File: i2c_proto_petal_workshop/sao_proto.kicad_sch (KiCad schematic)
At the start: 26 parts, among them J1 Simple_Addon_v2, J2 Programming: Jump Me, J3 GPIOs, J4 Jumpers, M1 Vibro Motor, M2 Solenoid, M3 Buzzer Motor, Q1 2N2222 (NPN), Q2 2N2222 (NPN), Q3 2N2222 (NPN)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

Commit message: updated schematic
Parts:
- added R6: 10K, symbol Device:R
- M1: value Vibro Motor -> Vibro Motor PWM
- M2: value Solenoid -> Solenoid GPIO Trigger
- M3: value Buzzer Motor -> Buzzer Motor GPIO
- R1: value 330R ? -> 68R ?
- R3: value 220R ? -> 1K
- R4: value 1K ? -> 1K
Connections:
- net PC0: now also J1.6 (GPIO2); no longer J1.5 (GPIO1), J2.2 (Pin_2)
- net PC3: no longer U1.13 (PC3)
- net PD5: no longer SW1.2
- net PD7: now also SW1.2, R6.2
- net VCC: now also R6.1
- net at J3.1 (Pin_1), R5.1: now also J1.5 (GPIO1), J2.2 (Pin_2); no longer J1.6 (GPIO2)
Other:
- note added: "CH32V003 Pin config: PC0 GPIO 2 input from Rpi (record signal), triggers in code RED LED on PD0 PC4 Vibro Output PC5 Solenoid Ouput PC6 Buzzer Output PD0 REC LED output (hardwired) PD1 PROGRAMMING input (hardwired) PD7 Push button input (pulled up with 10K resistor) GPIO 1 output from Rpi (metro signal) - doesn't come into the board, it just triggers the metronome LED"
- note added: "Solenoid currently unused!"
- note removed: "CH32V003 Pin config: PC0 GPIO 1 input from Rpi (record signal) PC4 Vibro Input PC5 Solenoid Input PC6 Buzzer Input PD0 REC LED output (hardwired) PD1 PROGRAMMING input (hardwired) Note: GPIO 2 input from Rpi doesn't come into the board, it just triggers the metronome LED"
- moved on the sheet: D2, D3, D4, J3, M2, M3, Q2, Q3, R1, R3, SW1

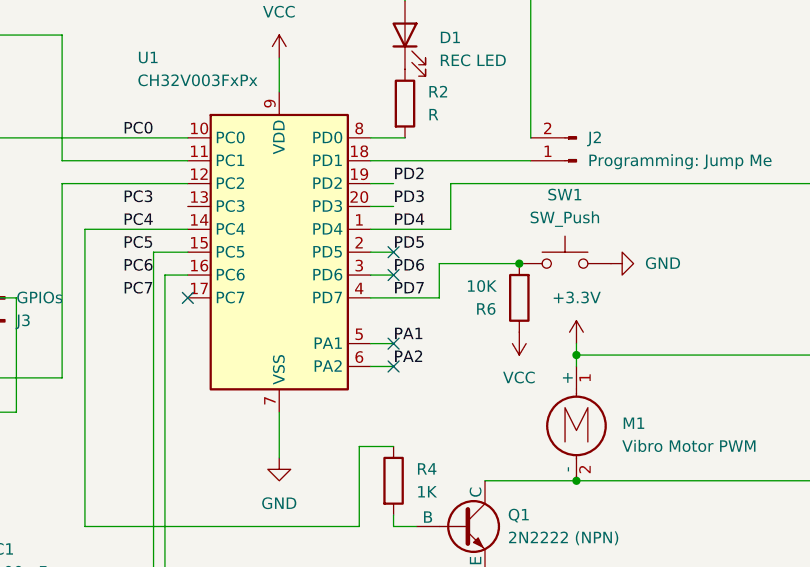
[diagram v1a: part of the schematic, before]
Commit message: moved button from PD7 to PD6 in schematic
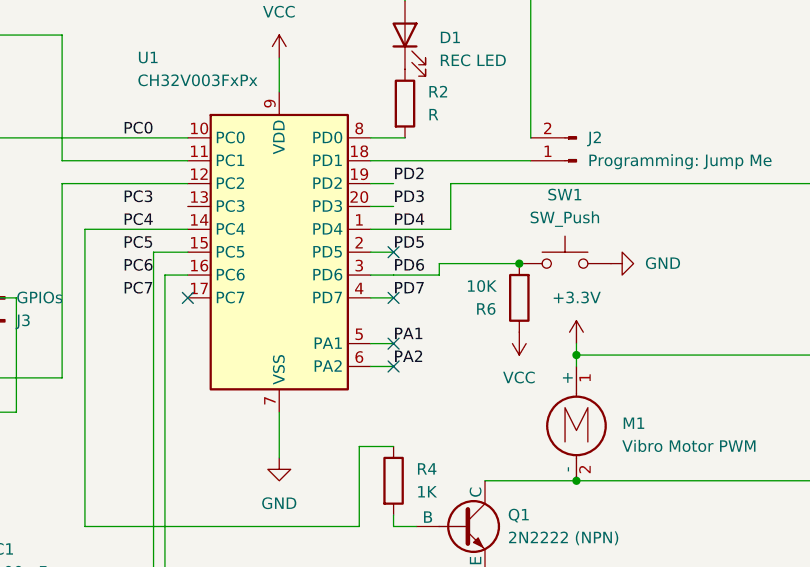
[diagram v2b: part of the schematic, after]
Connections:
- net PD6: now also R6.2, SW1.2
- net PD7: no longer R6.2, SW1.2

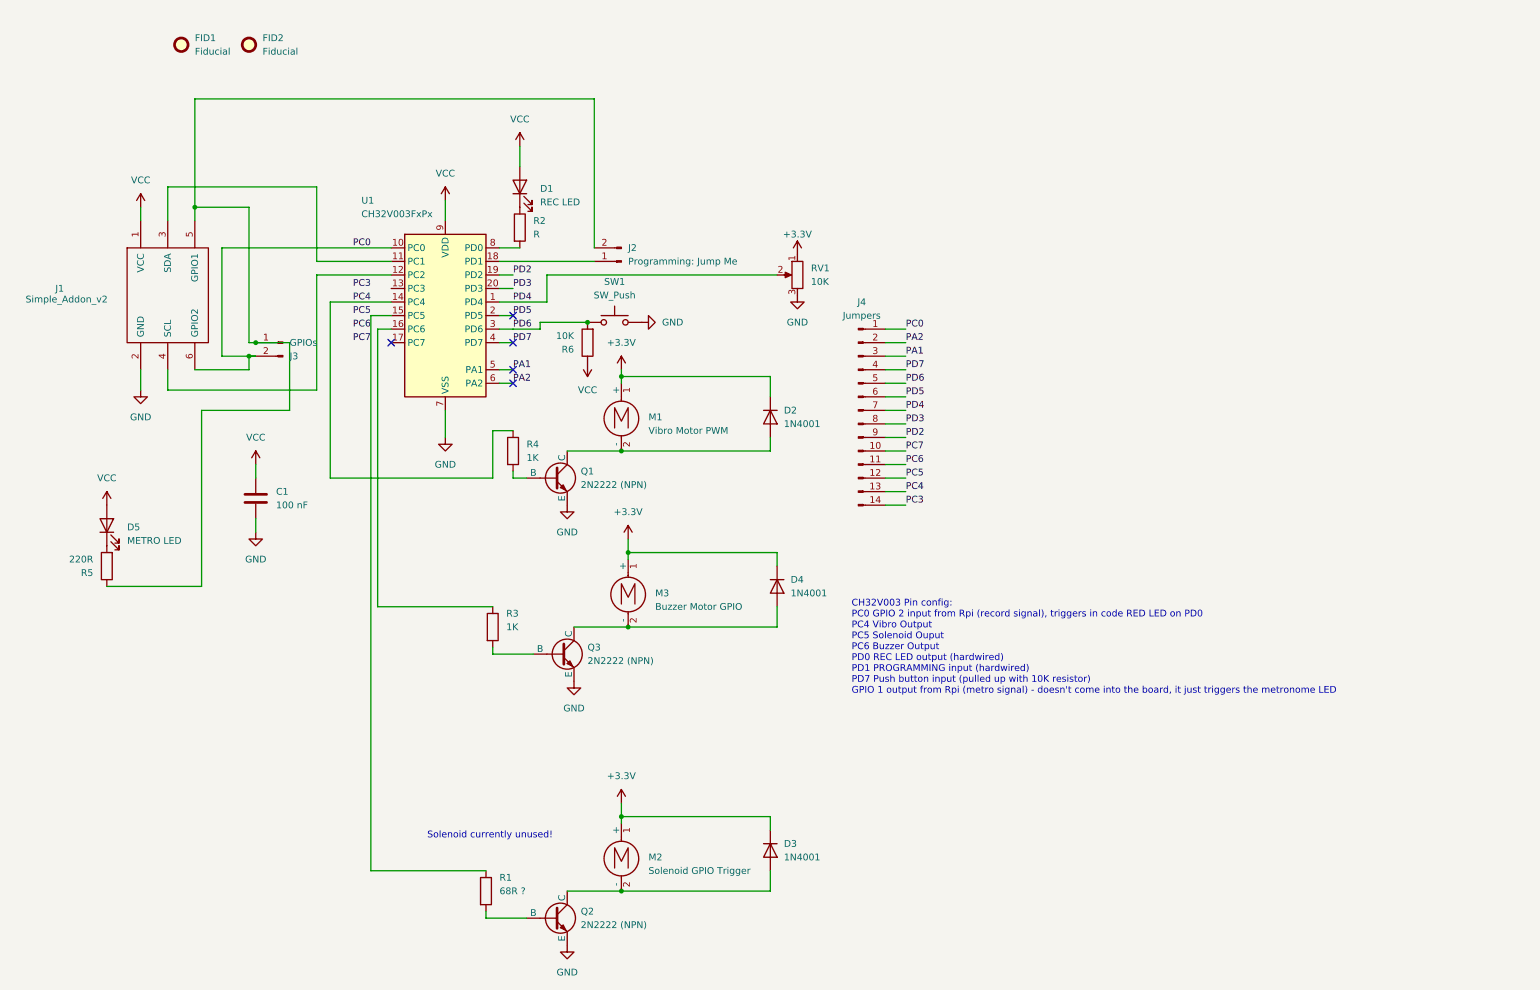
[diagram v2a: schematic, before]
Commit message: added Mitch's schematic revision, layout images and 3D step file for the potentiometer
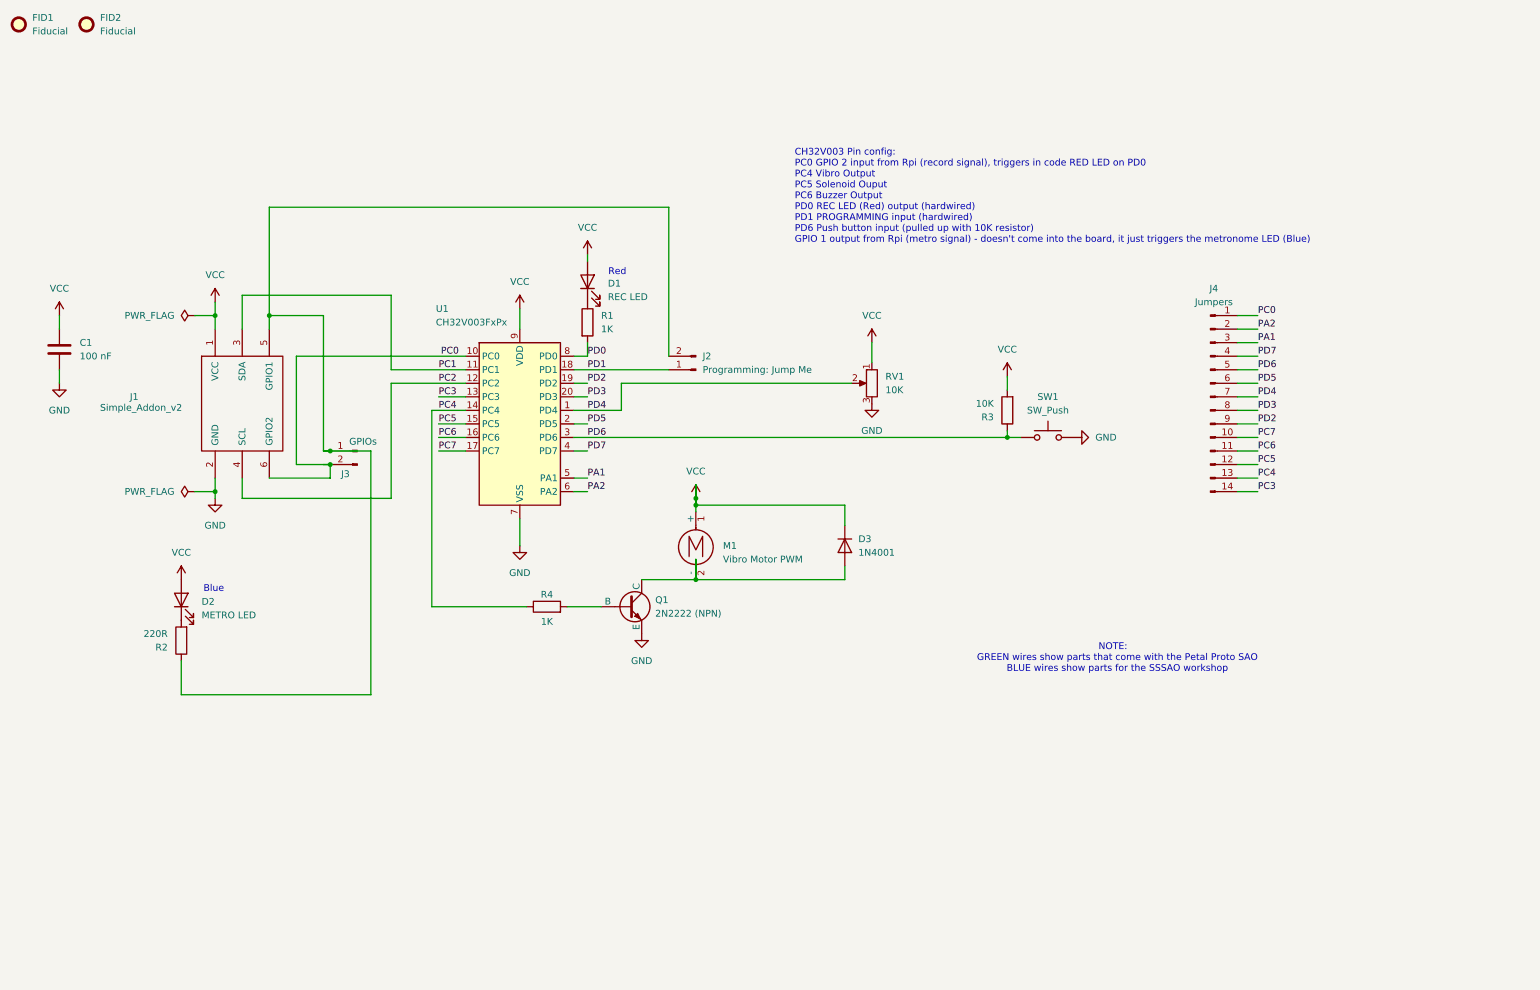
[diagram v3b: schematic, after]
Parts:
- removed D3, D4: 1N4001, Diode_THT:D_DO-41_SOD81_P10.16mm_Horizontal, symbol Diode:1N4001
- removed M2: Solenoid GPIO Trigger, symbol Motor:Motor_DC
- removed M3: Buzzer Motor GPIO, symbol Motor:Motor_DC
- removed Q2, Q3: 2N2222 (NPN), symbol Simulation_SPICE:NPN
- removed R1: 68R ?, symbol Device:R
- removed R3: 1K, symbol Device:R
- D2: renamed from D5; footprint (none) -> LED_THT:LED_D5.0mm
- M1: footprint (none) -> Connector_PinHeader_1.00mm:PinHeader_1x02_P1.00mm_Vertical
- Q1: footprint (none) -> Package_TO_SOT_THT:TO-92_Inline_Wide
- R1: renamed from R2; value R -> 1K
- R2: renamed from R5; footprint (none) -> Resistor_THT:R_Axial_DIN0309_L9.0mm_D3.2mm_P12.70mm_Horizontal
- R3: renamed from R6; footprint (none) -> Resistor_THT:R_Axial_DIN0309_L9.0mm_D3.2mm_P12.70mm_Horizontal
- R4: footprint (none) -> Resistor_THT:R_Axial_DIN0309_L9.0mm_D3.2mm_P12.70mm_Horizontal
- RV1: footprint (none) -> Potentiometer_THT:Potentiometer_Alps_RK09Y11_Single_Horizontal
- SW1: footprint (none) -> Button_Switch_THT:SW_PUSH_6mm
- renumbered D2 to D3
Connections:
- net +3.3V is gone; now on net VCC: D3.1 (K), M1.1 (+), RV1.1
- net PC3: now also U1.13 (PC3)
- net PC5: no longer J4.10 (Pin_10), J4.11 (Pin_11)
- net PD6: now also R3.1; no longer R3.2
- net VCC: now also R3.2; no longer R3.1
- net PC6: now reaches U1.16 (PC6)
- net PC6: now also J4.11 (Pin_11)
- net PD0: now reaches R1.2, U1.8 (PD0)
- net PC1: now reaches J1.3 (SDA), U1.11 (PC1)
- net PC2: now reaches J1.4 (SCL), U1.12 (PC2)
- net PC7: now reaches U1.17 (PC7)
- net PC7: now also J4.10 (Pin_10)
- net PD1: now reaches J2.1 (Pin_1), U1.18 (PD1)
- no-connect marks 5 -> 0
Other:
- note added: "Blue"
- note added: "CH32V003 Pin config: PC0 GPIO 2 input from Rpi (record signal), triggers in code RED LED on PD0 PC4 Vibro Output PC5 Solenoid Ouput PC6 Buzzer Output PD0 REC LED (Red) output (hardwired) PD1 PROGRAMMING input (hardwired) PD6 Push button input (pulled up with 10K resistor) GPIO 1 output from Rpi (metro signal) - doesn't come into the board, it just triggers the metronome LED (Blue)"
- note added: "NOTE: GREEN wires show parts that come with the Petal Proto SAO BLUE wires show parts for the SSSAO workshop"
- note added: "Red"
- note removed: "CH32V003 Pin config: PC0 GPIO 2 input from Rpi (record signal), triggers in code RED LED on PD0 PC4 Vibro Output PC5 Solenoid Ouput PC6 Buzzer Output PD0 REC LED output (hardwired) PD1 PROGRAMMING input (hardwired) PD7 Push button input (pulled up with 10K resistor) GPIO 1 output from Rpi (metro signal) - doesn't come into the board, it just triggers the metronome LED"
- note removed: "Solenoid currently unused!"
- moved on the sheet: C1, D1, D2, D3, FID1, FID2, J1, J2, J3, J4, M1, Q1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
